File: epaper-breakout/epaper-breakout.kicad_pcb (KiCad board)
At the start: 2 copper layers, 59 parts, among them J1 ED097OC4, J2 USB_B_Micro, J3 Conn_01x10, Q1 IRLML6402, SW1 RESET, SW2 BOOT, U1 LT1086-3.3, U2 LT1945, U3 L7915, U4 L7815, U5 ESP32-WROOM-32, U6 CH330N, U7 LM358

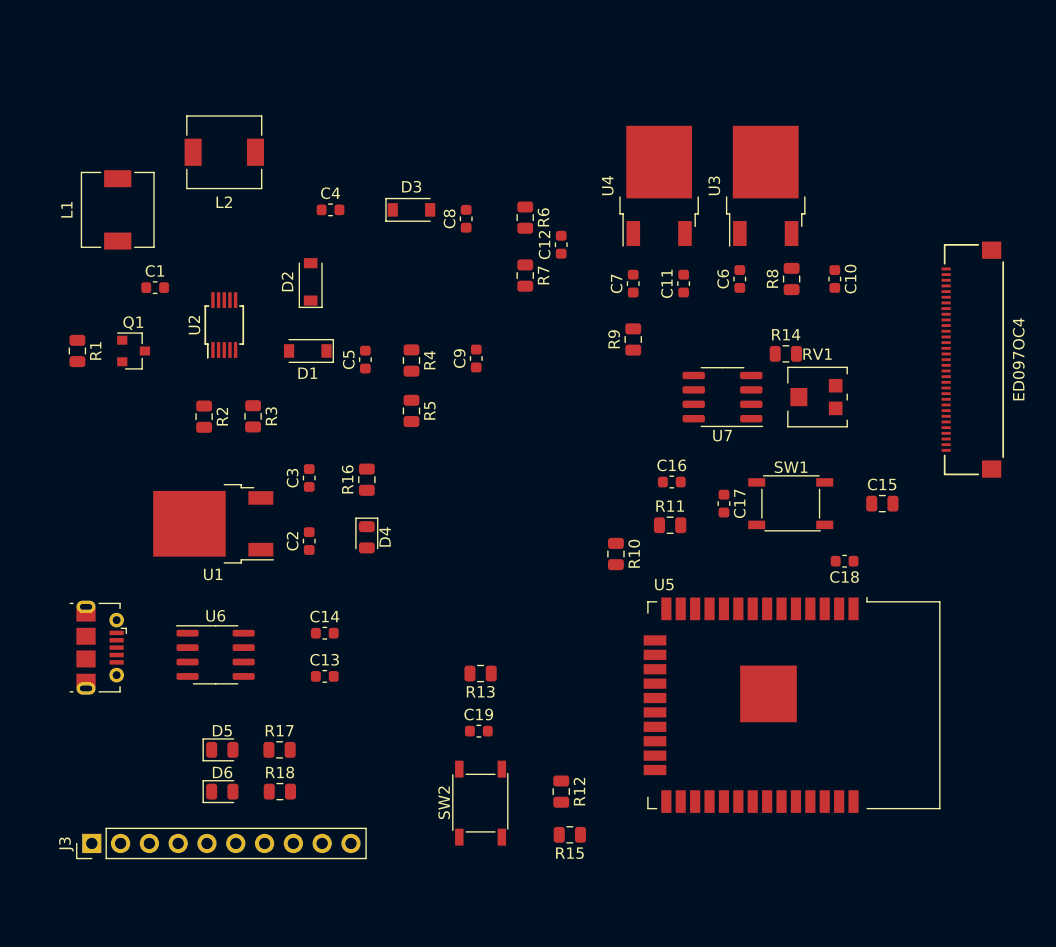
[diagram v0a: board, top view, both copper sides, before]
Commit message: fpc connector wiring
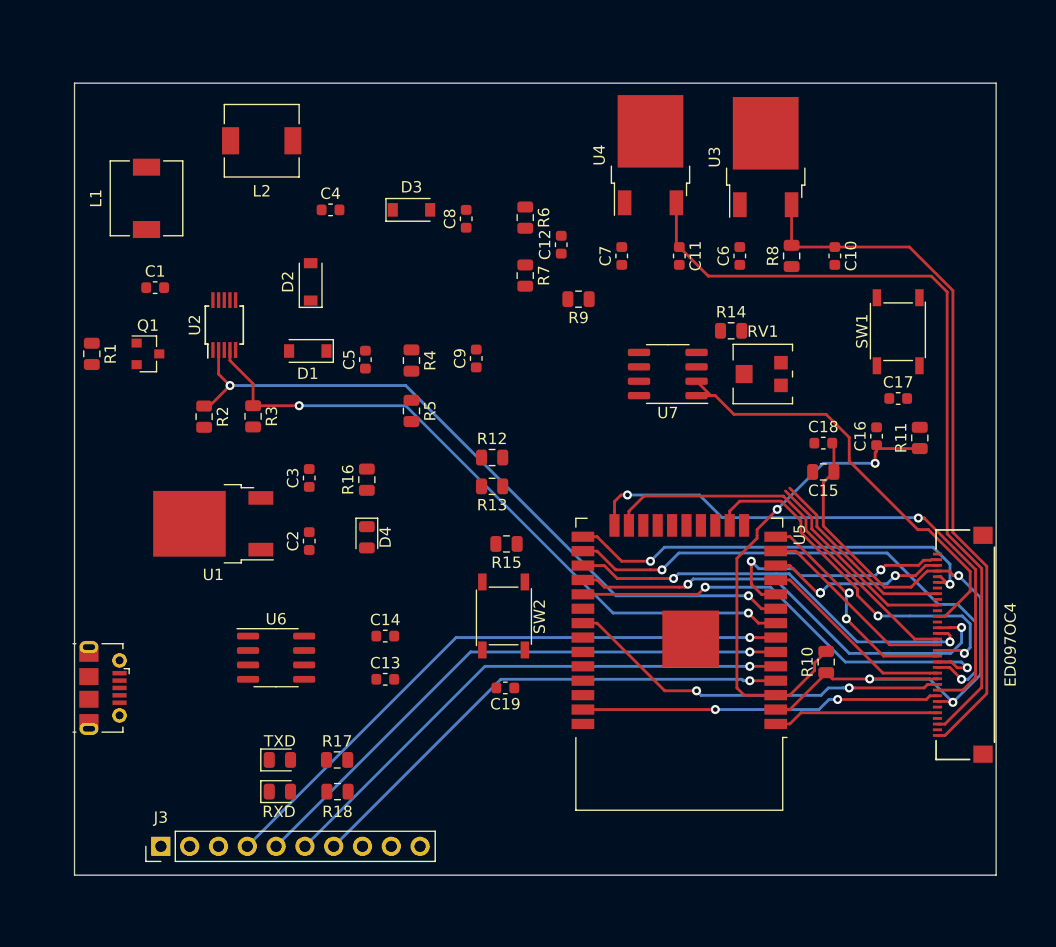
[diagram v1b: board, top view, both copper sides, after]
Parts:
- moved R12 30.1 mm to (88.1, -95.5), turned to 0 degrees
- moved R15 26.3 mm to (89.4, -87.9)
- moved J1 25.2 mm to (125.0, -79.0)
- moved R11 23.3 mm to (125.9, -97.2), turned to 90 degrees
- moved R10 20.8 mm to (117.6, -77.5), turned to 90 degrees
- moved C16 18.5 mm to (122.0, -97.4), turned to 90 degrees
- moved C17 17.9 mm to (124.0, -100.7), turned to 0 degrees
- moved SW1 17.9 mm to (124.0, -106.6), turned to 90 degrees
- moved SW2 16.6 mm to (89.2, -81.5), turned to 270 degrees
- moved R13 16.5 mm to (88.1, -93.0)
- moved C18 10.6 mm to (117.3, -96.8), turned to 0 degrees
- moved U5 9.71 mm to (104.6, -80.3), turned to 180 degrees
- moved J3 6.10 mm to (58.9, -61.2)
- moved R9 5.99 mm to (95.8, -109.5), turned to 180 degrees
- moved C15 5.91 mm to (117.3, -94.2), turned to 180 degrees
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- renumbered D6 to RXD, D5 to TXD
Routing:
- net /15V: track 0.00 -> 70.6 mm
- net /NEG_CTRL: track 0.00 -> 62.9 mm, vias 0 -> 2
- net /-15V: track 0.00 -> 62.1 mm
- net /+3.3V: track 0.00 -> 61.1 mm, vias 0 -> 3
- net /POS_CTRL: track 0.00 -> 59.8 mm, vias 0 -> 2
- net /A1: track 0.00 -> 54.2 mm, vias 0 -> 1
- net /A0: track 0.00 -> 51.2 mm, vias 0 -> 1
- net /EP_LE: track 0.00 -> 50.3 mm, vias 0 -> 2
- net /SENSOR_VN: track 0.00 -> 48.1 mm, vias 0 -> 1
- net /EP_D0: track 0.00 -> 46.9 mm, vias 0 -> 2
- net /SENSOR_VP: track 0.00 -> 45.1 mm, vias 0 -> 1
- net /EN: track 0.00 -> 43.2 mm, vias 0 -> 2
- net /EP_D7: track 0.00 -> 40.6 mm, vias 0 -> 2
- net /EP_D1: track 0.00 -> 40.0 mm, vias 0 -> 2
- net /EP_VCOM: track 0.00 -> 39.3 mm
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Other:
- board outline added: 81.3 x 69.8 mm

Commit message: initial wiring
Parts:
- moved C2 18.3 mm to (54.3, -83.3), turned to 0 degrees
- moved C1 15.7 mm to (56.1, -126.0), turned to 180 degrees
- moved L2 13.3 mm to (56.1, -117.1), turned to 270 degrees
- moved L1 8.99 mm to (64.3, -124.5), turned to 180 degrees
- moved R18 6.12 mm to (70.4, -70.6)
- moved RXD 6.12 mm to (65.4, -70.6)
- moved R13 5.93 mm to (94.0, -94.0)
- moved R17 4.44 mm to (70.4, -67.1)
- moved TXD 4.44 mm to (65.4, -67.1)
- moved D2 4.17 mm to (75.4, -113.5)
- moved C3 3.25 mm to (72.1, -90.4)
- moved R5 3.20 mm to (84.1, -100.6), turned to 0 degrees
- moved R9 3.05 mm to (95.8, -106.4)
- moved C4 3.05 mm to (71.1, -116.1), turned to 180 degrees
- moved D1 2.90 mm to (71.1, -107.7)
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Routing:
- net /+3.3V: track 61.1 -> 189.5 mm
- net /+22V: track 18.2 -> 86.3 mm, vias 0 -> 2
- net /-20V: track 17.5 -> 84.4 mm, vias 0 -> 2
- net /USB_TXD: track 0.00 -> 57.3 mm, vias 0 -> 2
- net /~SMPS_CTRL: track 0.00 -> 55.8 mm, vias 0 -> 2
- net Net-(C1-Pad1): track 0.00 -> 49.0 mm
- net /USB_RXD: track 0.00 -> 48.9 mm, vias 0 -> 2
- net /5V: track 0.00 -> 46.5 mm
- net /SCL: track 0.00 -> 46.4 mm, vias 0 -> 1
- net /SDA: track 0.00 -> 44.8 mm, vias 0 -> 1
- net Net-(C8-Pad1): track 0.00 -> 39.8 mm, vias 0 -> 2
- net Net-(C5-Pad1): track 0.00 -> 26.4 mm
- net /-15V: track 62.1 -> 83.1 mm, vias 0 -> 2
- net Net-(D1-Pad2): track 0.00 -> 20.8 mm
- net Net-(J2-Pad2): track 0.00 -> 18.9 mm
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
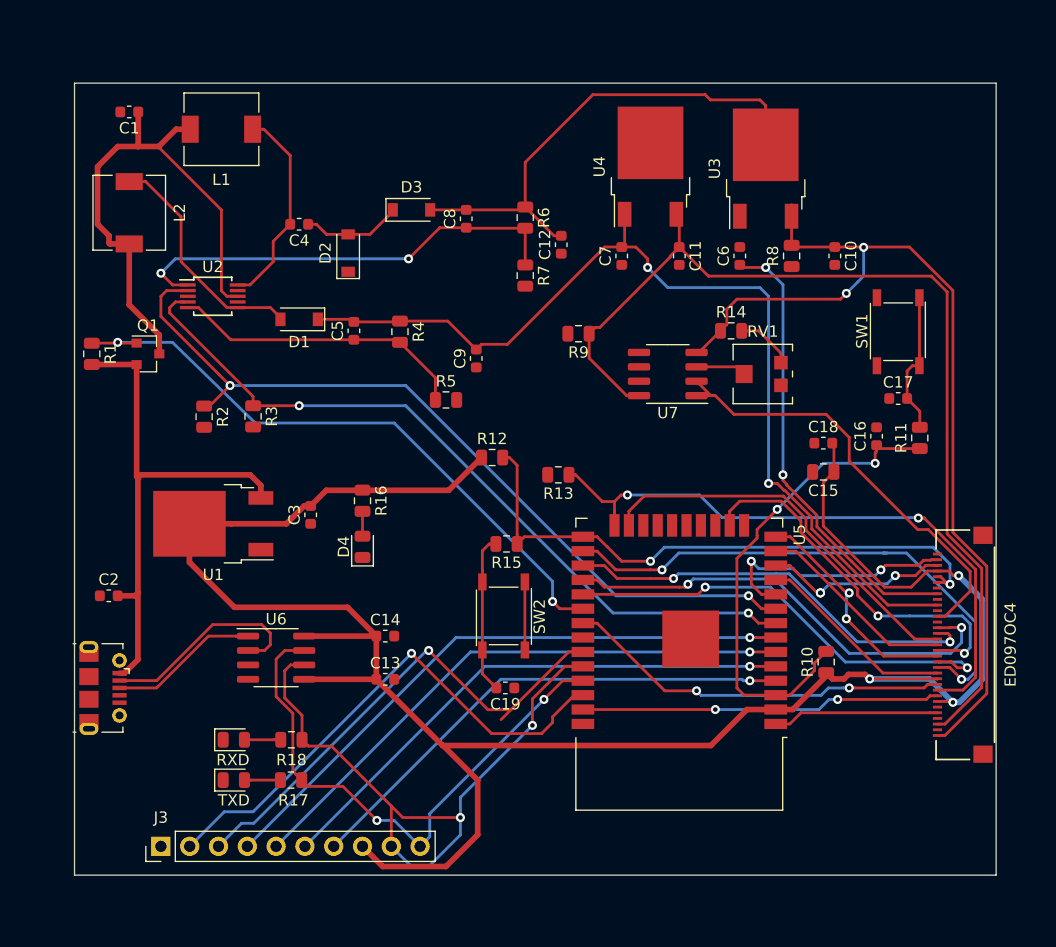
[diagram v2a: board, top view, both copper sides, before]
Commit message: fix drc problems
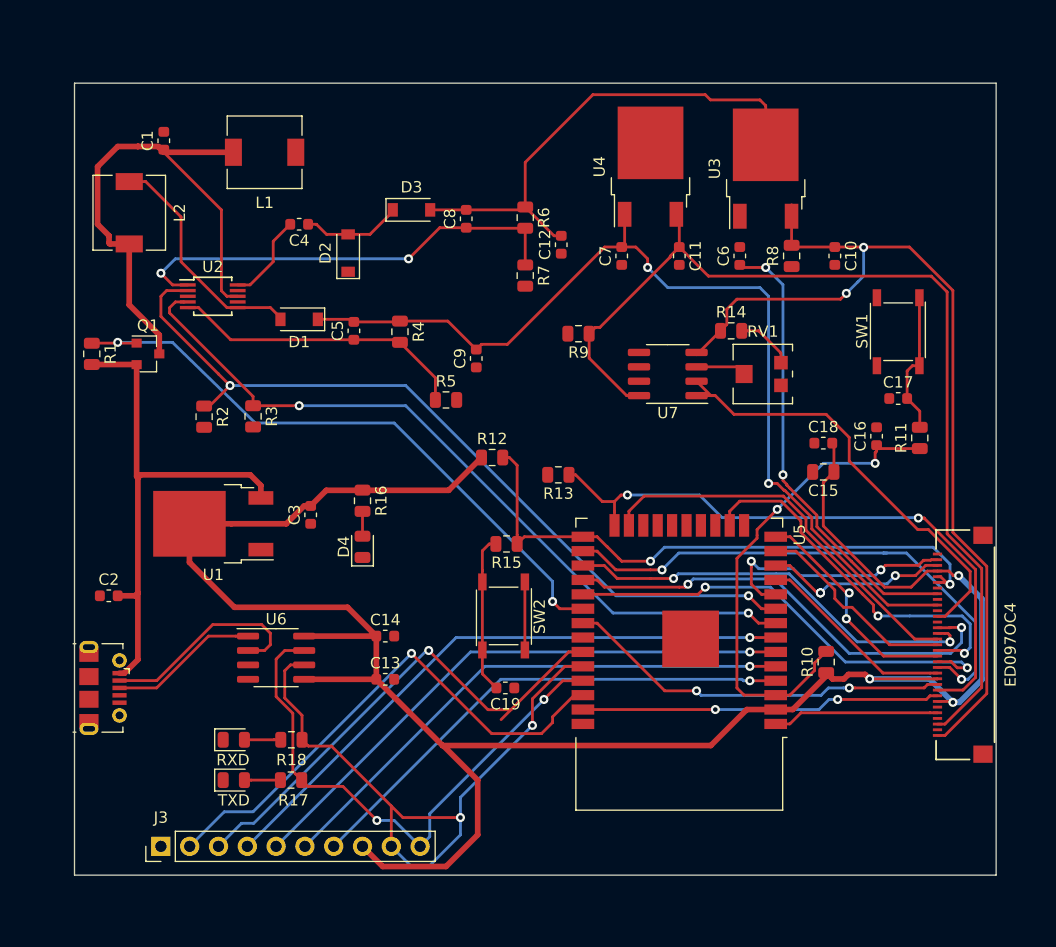
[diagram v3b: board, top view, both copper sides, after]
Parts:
- moved L1 4.32 mm to (68.1, -122.4)
- moved C1 3.97 mm to (59.2, -123.4), turned to 90 degrees
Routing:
- net Net-(C4-Pad2): track 18.2 -> 7.91 mm
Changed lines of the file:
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@@
     (thickness 1.6)
     (drawings 4)
-    (tracks 685)
+    (tracks 687)
     (zones 0)
     (modules 59)
@@
   )
   (module Inductor_SMD:L_6.3x6.3_H3 (layer F.Cu)
-    (at 64.262 -124.46 180)
+    (at 68.072 -122.428 180)
     (descr "Choke, SMD, 6.3x6.3mm 3mm height")
     (tags "Choke SMD")
@@
   )
   (module Capacitor_SMD:C_0603_1608Metric (layer F.Cu)
-    (at 56.134 -125.984 180)
+    (at 59.182 -123.444 90)
     (descr "Capacitor SMD 0603 (1608 Metric), square (rectangular) end terminal, IPC_7351 nominal, (Body size source: http://www.tortai-tech.com/upload/download/2011102023233369053.pdf), generated with kicad-footprint-generator")
     (tags capacitor)
     (attr smd)
-    (fp_text reference C1 (at 0 -1.43) (layer F.SilkS)
+    (fp_text reference C1 (at 0 -1.43 90) (layer F.SilkS)
       (effects (font (size 1 1) (thickness 0.15)))
     )
-    (fp_text value 4.7uF (at 0 1.43) (layer F.Fab)
+    (fp_text value 4.7uF (at 0 1.43 90) (layer F.Fab)
       (effects (font (size 1 1) (thickness 0.15)))
     )
-    (fp_text user %R (at 0 0) (layer F.Fab)
+    (fp_text user %R (at 0 0 90) (layer F.Fab)
       (effects (font (size 0.4 0.4) (thickness 0.06)))
     )
@@
     (fp_line (start -0.8 -0.4) (end 0.8 -0.4) (layer F.Fab) (width 0.1))
     (fp_line (start -0.8 0.4) (end -0.8 -0.4) (layer F.Fab) (width 0.1))
-    (pad 2 smd roundrect (at 0.7875 0 180) (size 0.875 0.95) (layers F.Cu F.Paste F.Mask) (roundrect_rratio 0.25)
+    (pad 2 smd roundrect (at 0.7875 0 90) (size 0.875 0.95) (layers F.Cu F.Paste F.Mask) (roundrect_rratio 0.25)
       (net 1 GND))
-    (pad 1 smd roundrect (at -0.7875 0 180) (size 0.875 0.95) (layers F.Cu F.Paste F.Mask) (roundrect_rratio 0.25)
+    (pad 1 smd roundrect (at -0.7875 0 90) (size 0.875 0.95) (layers F.Cu F.Paste F.Mask) (roundrect_rratio 0.25)
       (net 2 "Net-(C1-Pad1)"))
     (model ${KISYS3DMOD}/Capacitor_SMD.3dshapes/C_0603_1608Metric.wrl
@@
   (segment (start 54.434 -114.344) (end 56.134 -114.344) (width 0.5) (layer F.Cu) (net 2))
   (segment (start 53.34 -116.078) (end 54.356 -115.062) (width 0.5) (layer F.Cu) (net 2))
-  (segment (start 61.512 -124.46) (end 60.262 -124.46) (width 0.5) (layer F.Cu) (net 2))
   (segment (start 54.356 -114.422) (end 54.434 -114.344) (width 0.5) (layer F.Cu) (net 2))
   (segment (start 55.118 -122.936) (end 53.34 -121.158) (width 0.5) (layer F.Cu) (net 2))
-  (segment (start 60.262 -124.46) (end 58.738 -122.936) (width 0.5) (layer F.Cu) (net 2))
   (segment (start 53.34 -121.158) (end 53.34 -116.078) (width 0.5) (layer F.Cu) (net 2))
-  (segment (start 56.9215 -125.984) (end 56.9215 -122.9615) (width 0.5) (layer F.Cu) (net 2))
   (segment (start 58.738 -122.936) (end 56.896 -122.936) (width 0.5) (layer F.Cu) (net 2))
   (segment (start 56.9215 -122.9615) (end 56.896 -122.936) (width 0.5) (layer F.Cu) (net 2))
@@
   (segment (start 64.262 -110.216) (end 64.75 -109.728) (width 0.25) (layer F.Cu) (net 2))
   (segment (start 64.262 -117.348) (end 64.262 -110.216) (width 0.25) (layer F.Cu) (net 2))
+  (segment (start 59.182 -122.428) (end 65.322 -122.428) (width 0.5) (layer F.Cu) (net 2))
+  (segment (start 58.738 -122.872) (end 59.182 -122.428) (width 0.5) (layer F.Cu) (net 2))
   (segment (start 67.744 -93.043) (end 67.744 -91.943) (width 0.5) (layer F.Cu) (net 3))
   (segment (start 66.807 -93.98) (end 67.744 -93.043) (width 0.5) (layer F.Cu) (net 3))
@@
   (segment (start 68.834 -114.5795) (end 70.3325 -116.078) (width 0.25) (layer F.Cu) (net 5))
   (segment (start 68.834 -112.776) (end 68.834 -114.5795) (width 0.25) (layer F.Cu) (net 5))
-  (segment (start 68.012 -124.46) (end 67.012 -124.46) (width 0.25) (layer F.Cu) (net 5))
-  (segment (start 70.3325 -122.1395) (end 68.012 -124.46) (width 0.25) (layer F.Cu) (net 5))
-  (segment (start 70.3325 -116.078) (end 70.3325 -122.1395) (width 0.25) (layer F.Cu) (net 5))
   (segment (start 71.9075 -116.078) (end 72.644 -116.078) (width 0.25) (layer F.Cu) (net 6))
   (segment (start 73.534 -115.188) (end 75.438 -115.188) (width 0.25) (layer F.Cu) (net 6))
@@
   (segment (start 124.968 -81.534) (end 122.174 -81.534) (width 0.25) (layer B.Cu) (net 30))
   (segment (start 122.174 -81.534) (end 122.174 -81.534) (width 0.25) (layer B.Cu) (net 30))
-  (via (at 122.174 -81.534) (size 0.8) (drill 0.4) (layers F.Cu B.Cu) (net 30))
-  (segment (start 120.359001 -83.914001) (end 115.373002 -88.9) (width 0.25) (layer F.Cu) (net 30))
-  (segment (start 122.174 -81.534) (end 120.359001 -83.348999) (width 0.25) (layer F.Cu) (net 30))
-  (segment (start 120.359001 -83.348999) (end 120.359001 -83.914001) (width 0.25) (layer F.Cu) (net 30))
-  (segment (start 109.093 -90.769) (end 109.093 -89.519) (width 0.25) (layer F.Cu) (net 30))
+  (segment (start 121.774001 -81.933999) (end 121.774001 -82.499001) (width 0.25) (layer F.Cu) (net 30))
+  (segment (start 120.396 -83.877002) (end 115.373002 -88.9) (width 0.25) (layer F.Cu) (net 30))
   (segment (start 113.632001 -91.657001) (end 109.981001 -91.657001) (width 0.25) (layer F.Cu) (net 30))
+  (segment (start 122.174 -81.534) (end 121.774001 -81.933999) (width 0.25) (layer F.Cu) (net 30))
   (segment (start 115.373002 -89.916) (end 113.632001 -91.657001) (width 0.25) (layer F.Cu) (net 30))
-  (segment (start 109.981001 -91.657001) (end 109.093 -90.769) (width 0.25) (layer F.Cu) (net 30))
   (segment (start 115.373002 -88.9) (end 115.373002 -89.916) (width 0.25) (layer F.Cu) (net 30))
+  (segment (start 109.093 -90.769) (end 109.093 -89.519) (width 0.25) (layer F.Cu) (net 30))
+  (via (at 122.174 -81.534) (size 0.8) (drill 0.4) (layers F.Cu B.Cu) (net 30))
+  (segment (start 120.805501 -83.467501) (end 120.453002 -83.82) (width 0.25) (layer F.Cu) (net 30))
+  (segment (start 109.981001 -91.657001) (end 109.093 -90.769) (width 0.25) (layer F.Cu) (net 30))
+  (segment (start 121.774001 -82.499001) (end 120.805501 -83.467501) (width 0.25) (layer F.Cu) (net 30))
   (segment (start 113.148 -87.249) (end 114.935 -87.249) (width 0.25) (layer F.Cu) (net 31))
   (segment (start 123.19 -78.994) (end 127.4191 -78.994) (width 0.25) (layer F.Cu) (net 31))
-  (segment (start 114.935 -87.249) (end 123.19 -78.994) (width 0.25) (layer F.Cu) (net 31))
+  (segment (start 118.364 -83.82) (end 118.364 -83.058) (width 0.25) (layer F.Cu) (net 31))
+  (segment (start 114.935 -87.249) (end 118.364 -83.82) (width 0.25) (layer F.Cu) (net 31))
+  (segment (start 119.126 -82.296) (end 119.888 -82.296) (width 0.25) (layer F.Cu) (net 31))
+  (segment (start 118.364 -83.058) (end 119.126 -82.296) (width 0.25) (layer F.Cu) (net 31))
+  (segment (start 119.888 -82.296) (end 123.19 -78.994) (width 0.25) (layer F.Cu) (net 31))
   (segment (start 127.4191 -79.494002) (end 125.41541 -79.494002) (width 0.25) (layer F.Cu) (net 32))
   (segment (start 100.203 -90.769) (end 100.203 -89.519) (width 0.25) (layer F.Cu) (net 32))

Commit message: add screw holes
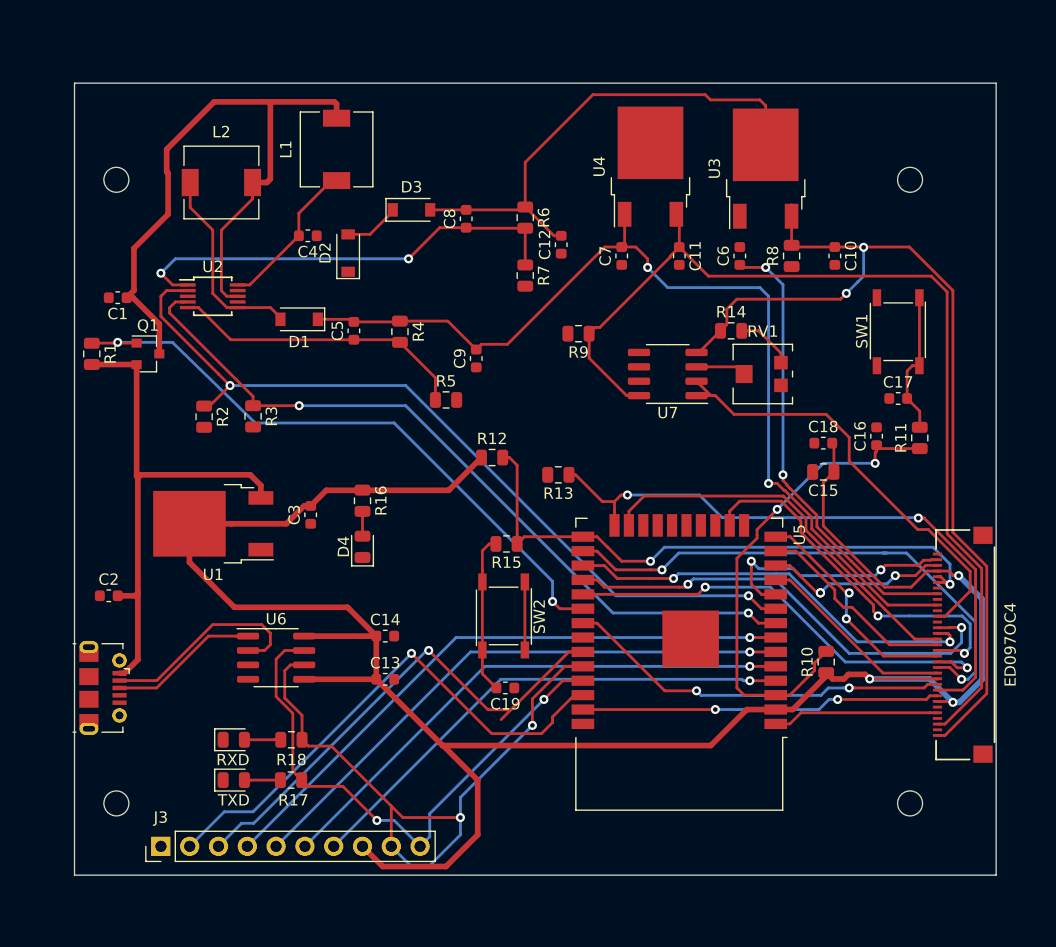
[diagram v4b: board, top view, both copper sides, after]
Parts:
- added REF**: MountingHole_2.2mm_M2, MountingHole:MountingHole_2.2mm_M2, F.Cu at (55.0, -120.0)
- added REF**: MountingHole_2.2mm_M2, MountingHole:MountingHole_2.2mm_M2, F.Cu at (55.0, -65.0)
- added REF**: MountingHole_2.2mm_M2, MountingHole:MountingHole_2.2mm_M2, F.Cu at (125.0, -65.0)
- added REF**: MountingHole_2.2mm_M2, MountingHole:MountingHole_2.2mm_M2, F.Cu at (125.0, -120.0)
- moved C1 14.4 mm to (55.1, -109.6), turned to 180 degrees
- moved L2 8.55 mm to (64.3, -119.8), turned to 0 degrees
- moved L1 6.36 mm to (74.4, -122.7), turned to 90 degrees
- moved C4 1.27 mm to (71.9, -115.1)
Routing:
- net Net-(C1-Pad1): track 49.3 -> 60.0 mm
- net Net-(C4-Pad2): track 7.91 -> 13.7 mm
- net Net-(C4-Pad1): track 8.82 -> 4.92 mm
- net Net-(D1-Pad2): track 20.8 -> 17.6 mm
